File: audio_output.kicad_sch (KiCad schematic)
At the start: 33 parts, among them J10 NCJ6FA-H-0, J9 NCJ6FA-H-0, U4 OPA1656ID, U5 THAT1646, U6 THAT1646

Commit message: final layout
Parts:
- renumbered C19 to C1, C12 to C10, C24 to C11, C14 to C13, C17 to C15, C15 to C16, C21 to C2, C18 to C3, C20 to C4, C23 to C5, C25 to C6, C22 to C7, C16 to C8, C13 to C9, D6 to D1, D10 to D2, D13 to D3, D11 to D4, D12 to D5, D7 to D6, D8 to D7, D9 to D8, J9 to J1, J10 to J2, R21 to R2, R19 to R5, R20 to R6, R22 to R7, RV1 to RV2, RV2 to RV4, U5 to U1, U6 to U2, U4 to U3

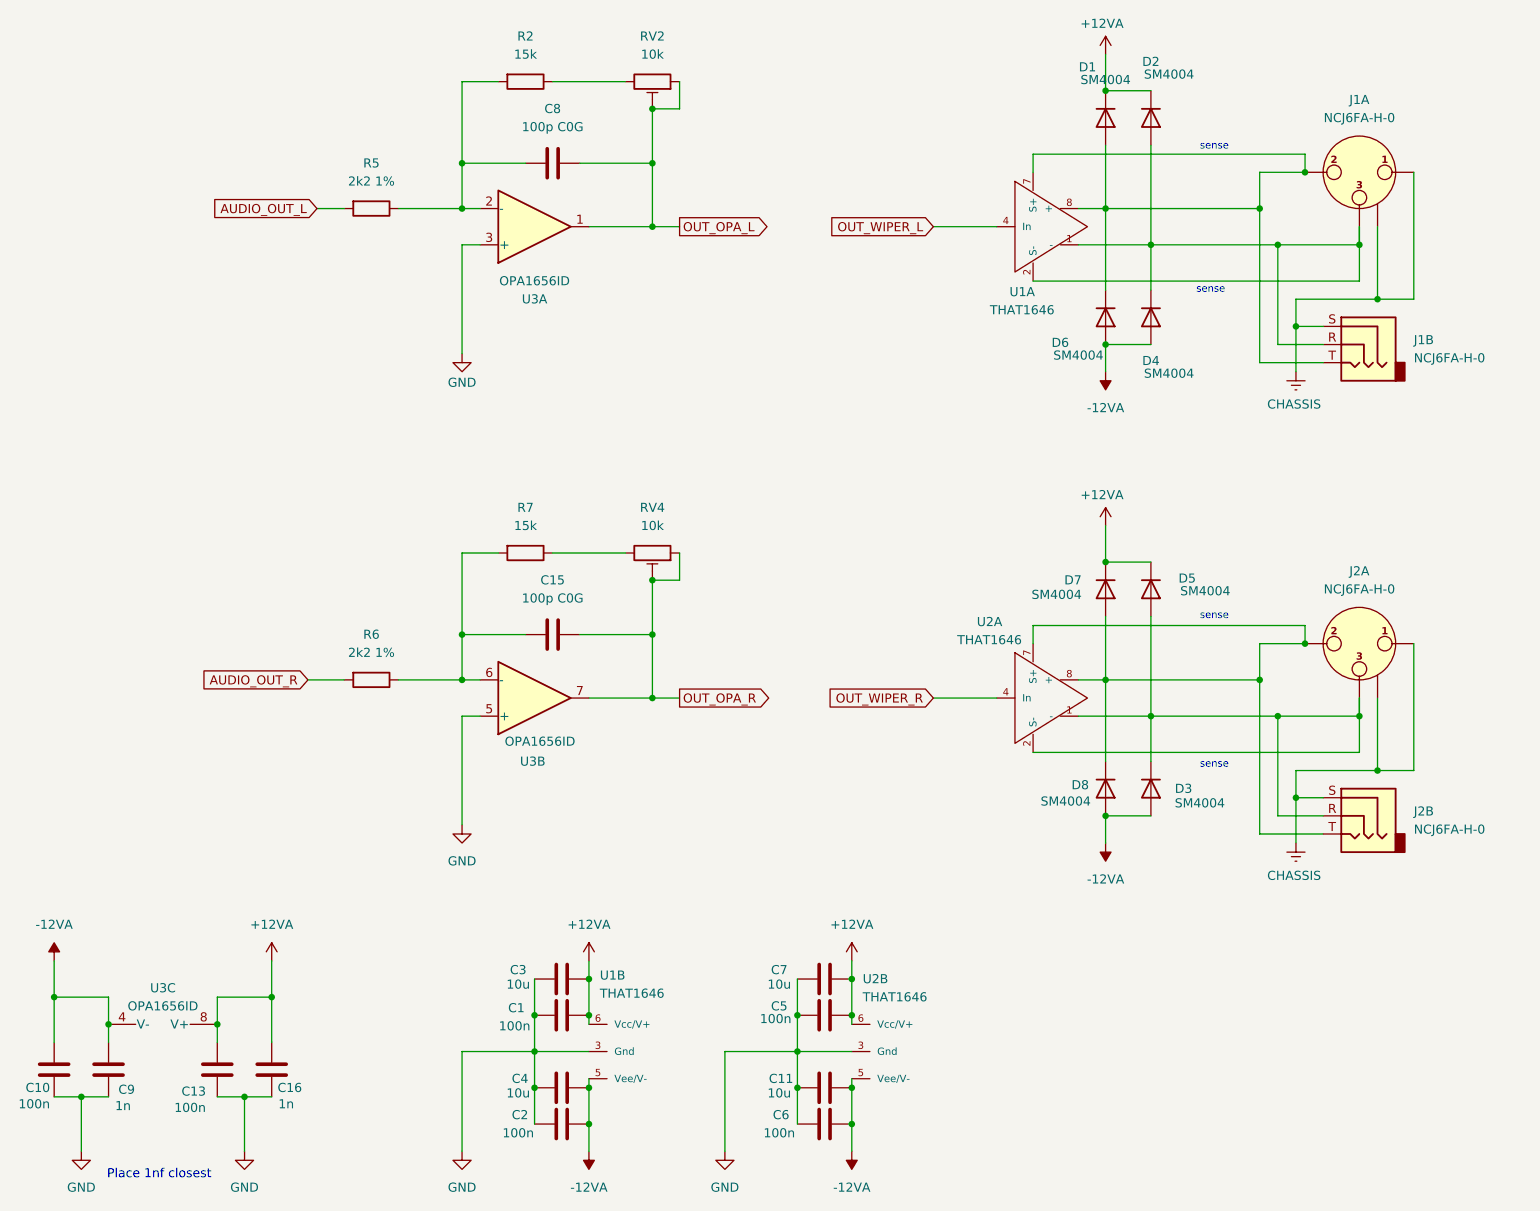
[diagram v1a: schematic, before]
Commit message: added 3d models
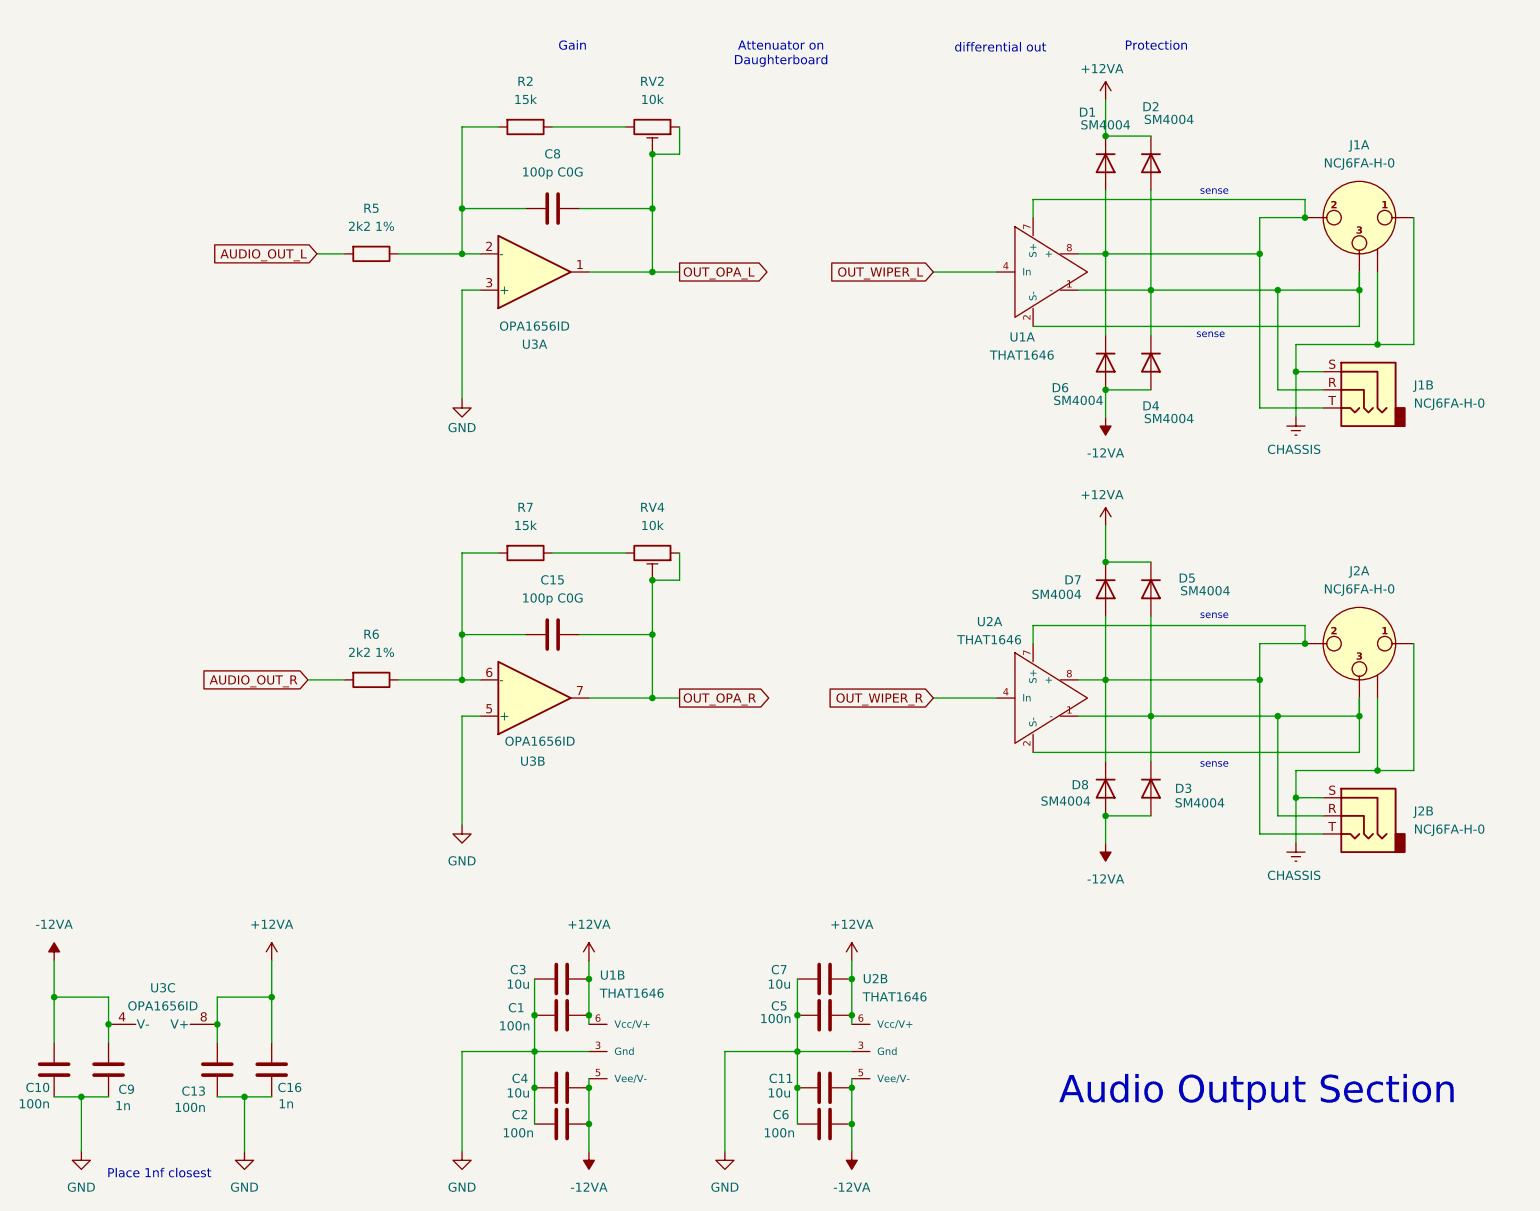
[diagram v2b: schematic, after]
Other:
- note added: "Attenuator on Daughterboard"
- note added: "Audio Output Section"
- note added: "Gain"
- note added: "Protection"
- note added: "differential out"
- moved on the sheet: C8, D1, D2, D4, D6, J1A, J1B, R2, R5, RV2, U1A, U3A

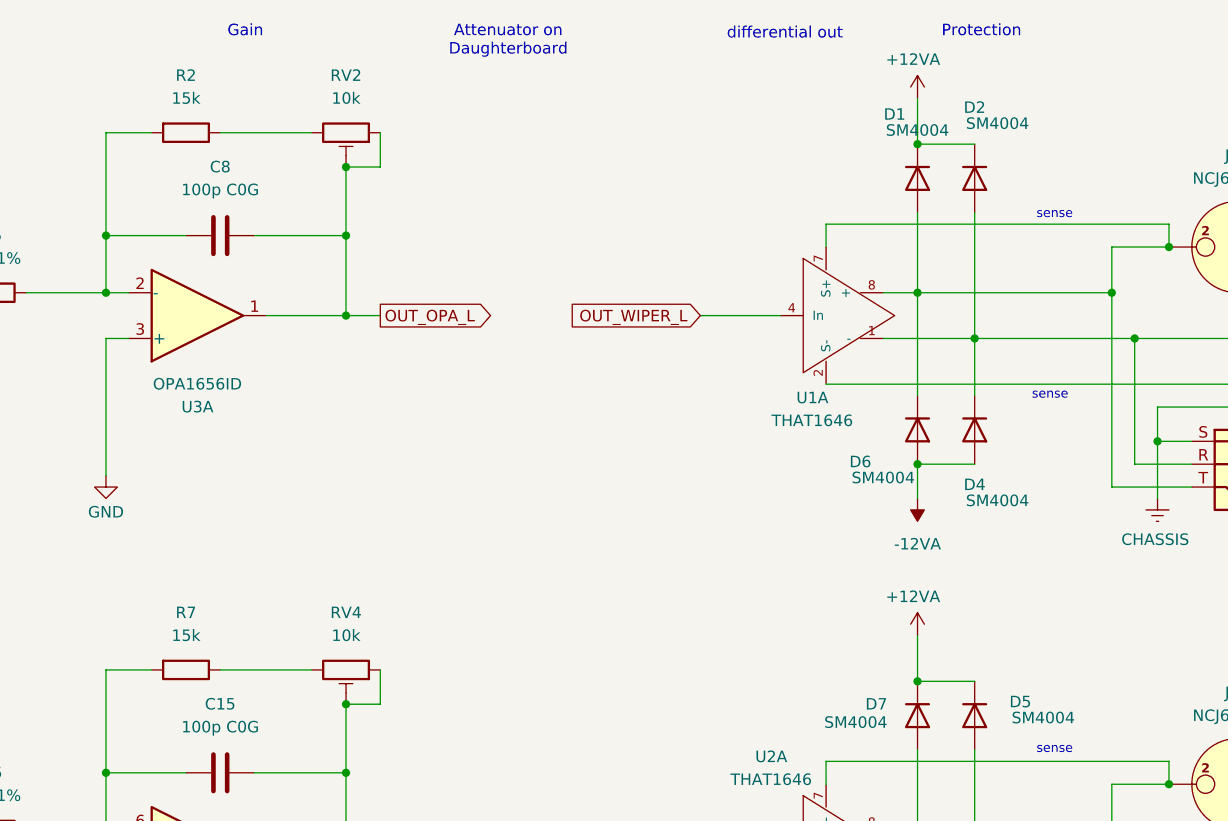
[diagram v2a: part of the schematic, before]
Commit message: r_fb_fixed changed to 6.8k
closes #15
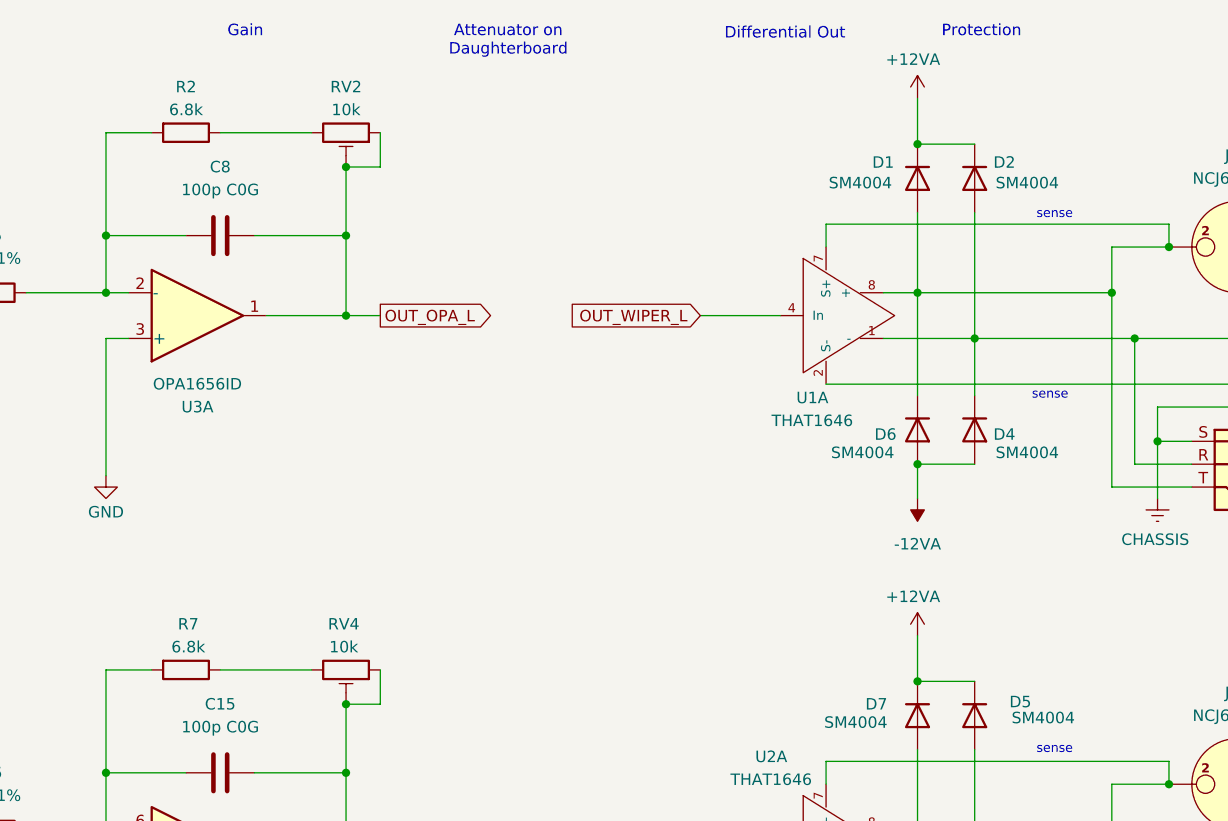
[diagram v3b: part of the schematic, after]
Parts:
- R2, R7: value 15k -> 6.8k
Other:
- note added: "Differential Out"
- note removed: "differential out"
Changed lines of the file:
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@@
 		)
 	)
-	(text "differential out\n"
+	(text "Differential Out"
 		(exclude_from_sim no)
 		(at 156.718 30.988 0)
@@
 		(on_board yes)
 		(dnp no)
-		(fields_autoplaced yes)
 		(property "Reference" "R7"
-			(at 90.17 95.25 90)
+			(at 90.424 96.52 90)
 			(effects
 				(font
@@
 			)
 		)
-		(property "Value" "15k"
-			(at 90.17 97.79 90)
+		(property "Value" "6.8k"
+			(at 90.424 99.06 90)
 			(effects
 				(font
@@
 		(dnp no)
 		(property "Reference" "D6"
-			(at 165.1 78.486 90)
+			(at 167.894 75.438 90)
 			(effects
 				(font
@@
 		)
 		(property "Value" "SM4004"
-			(at 167.64 80.264 90)
+			(at 165.354 77.47 90)
 			(effects
 				(font
@@
 		(dnp no)
 		(property "Reference" "D2"
-			(at 177.8 39.116 90)
+			(at 181.102 45.212 90)
 			(effects
 				(font
@@
 		)
 		(property "Value" "SM4004"
-			(at 180.34 40.894 90)
+			(at 183.642 47.498 90)
 			(effects
 				(font
@@
 		(on_board yes)
 		(dnp no)
-		(fields_autoplaced yes)
 		(property "Reference" "R2"
-			(at 90.17 35.56 90)
+			(at 90.17 36.83 90)
 			(effects
 				(font
@@
 			)
 		)
-		(property "Value" "15k"
-			(at 90.17 38.1 90)
+		(property "Value" "6.8k"
+			(at 90.17 39.37 90)
 			(effects
 				(font
@@
 		(on_board yes)
 		(dnp no)
-		(fields_autoplaced yes)
 		(property "Reference" "RV2"
-			(at 107.95 35.56 90)
+			(at 107.95 36.83 90)
 			(effects
 				(font
@@
 		)
 		(property "Value" "10k"
-			(at 107.95 38.1 90)
+			(at 107.95 39.37 90)
 			(effects
 				(font
@@
 		(on_board yes)
 		(dnp no)
-		(fields_autoplaced yes)
 		(property "Reference" "RV4"
-			(at 107.95 95.25 90)
+			(at 107.696 96.52 90)
 			(effects
 				(font
@@
 		)
 		(property "Value" "10k"
-			(at 107.95 97.79 90)
+			(at 107.696 99.06 90)
 			(effects
 				(font
@@
 		(dnp no)
 		(property "Reference" "D4"
-			(at 177.8 81.026 90)
+			(at 181.102 75.438 90)
 			(effects
 				(font
@@
 		)
 		(property "Value" "SM4004"
-			(at 180.34 82.804 90)
+			(at 183.642 77.47 90)
 			(effects
 				(font
@@
 		(dnp no)
 		(property "Reference" "D1"
-			(at 168.91 39.878 90)
+			(at 167.64 45.212 90)
 			(effects
 				(font
@@
 		)
 		(property "Value" "SM4004"
-			(at 171.45 41.656 90)
+			(at 165.1 47.498 90)
 			(effects
 				(font
